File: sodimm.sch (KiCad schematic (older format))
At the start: 1 part, among them J5 2309409-1

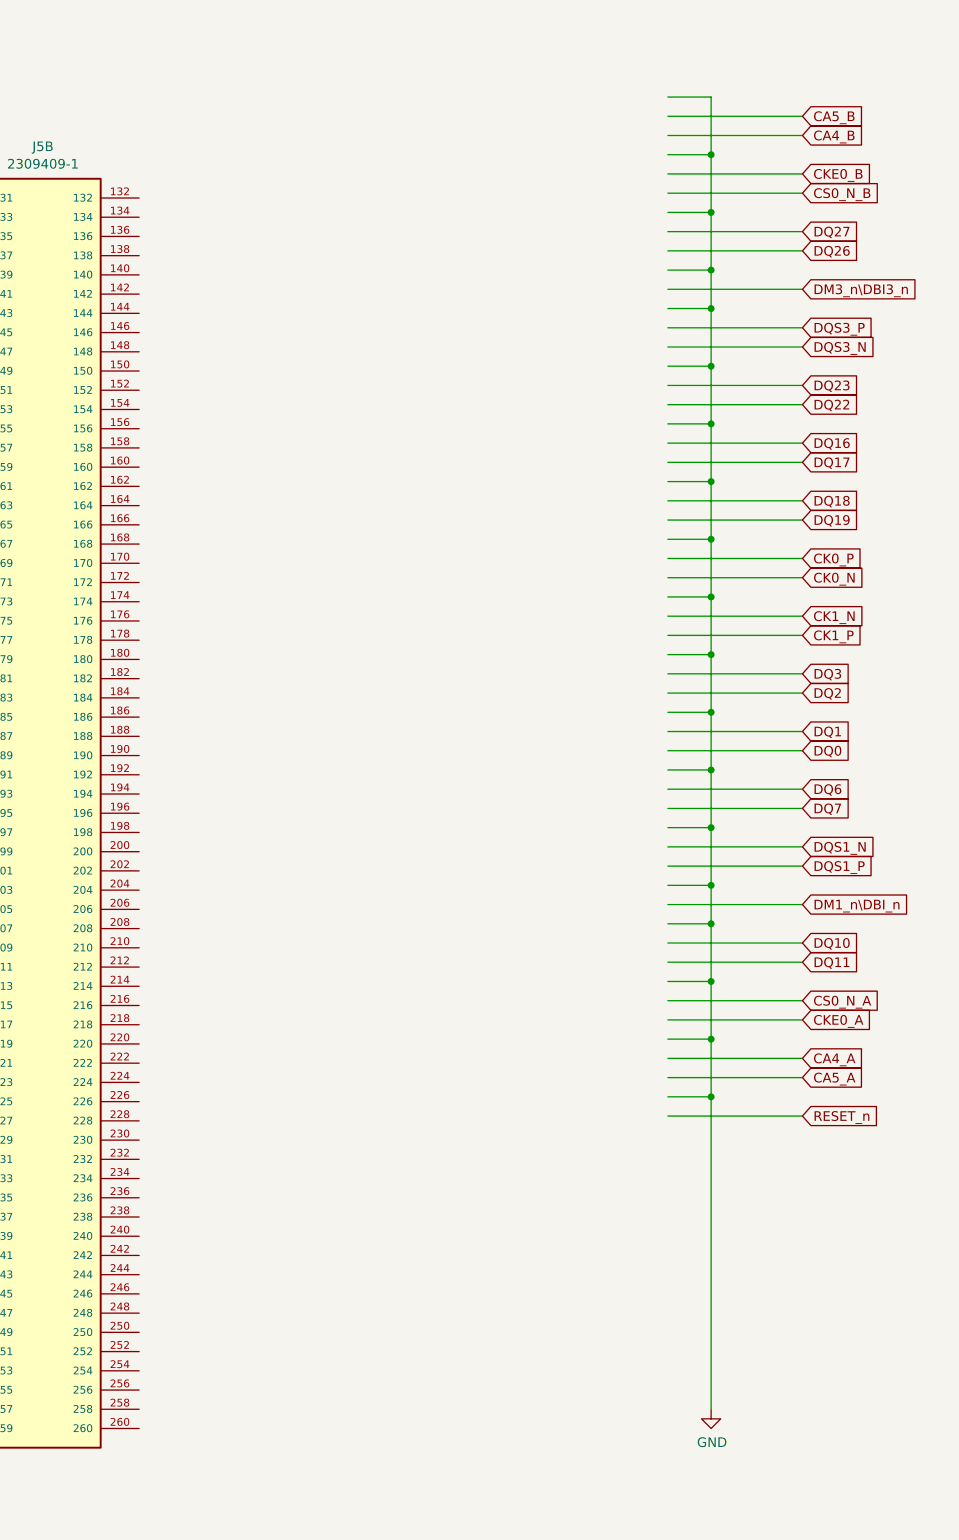
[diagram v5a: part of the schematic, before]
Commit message: Connect CA and spare IOs to SODIMM
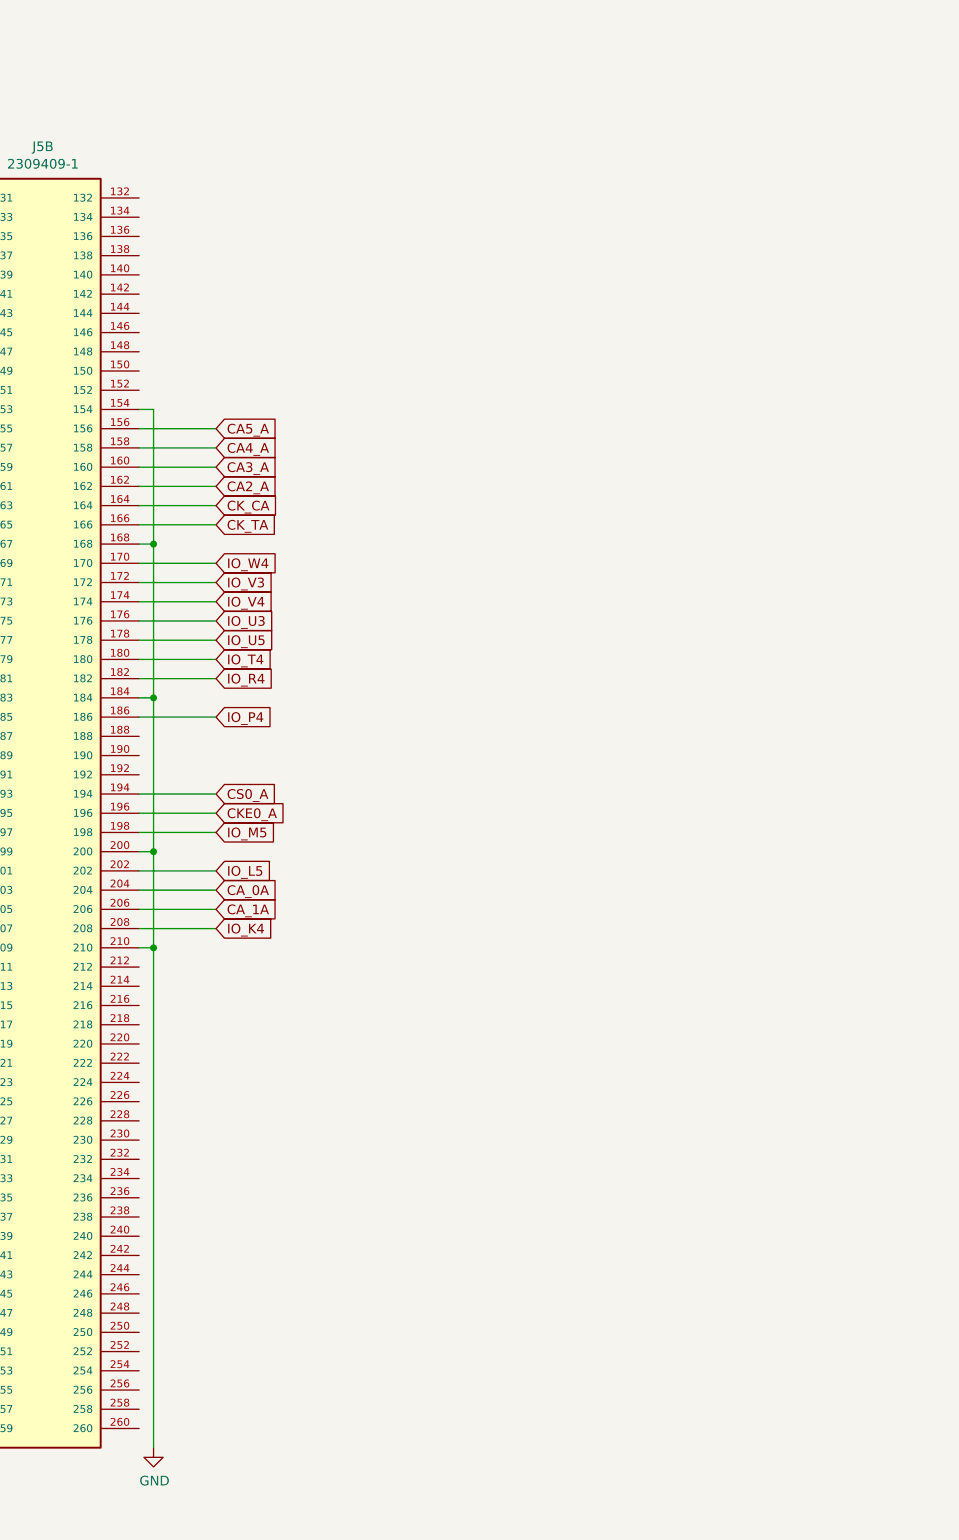
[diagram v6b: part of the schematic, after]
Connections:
- net labels added: CA_0A, CA_1A, CK_CA, CK_TA, CS0_A, IO_K4, IO_L5, IO_M5, IO_P4, IO_R4, IO_T4, IO_U3, IO_U5, IO_V3, IO_V4, IO_W4
- net labels removed: CA4_B, CA5_B, CK0_N, CK0_P, CK1_N, CK1_P, CKE0_B, CS0_N_A, CS0_N_B, DM1_n\DBI_n, DM3_n\DBI3_n, DQ0, DQ1, DQ10, DQ11, DQ16, DQ17, DQ18, DQ19, DQ2, DQ22, DQ23, DQ26, DQ27, DQ3, DQ6, DQ7, DQS1_N, DQS1_P, DQS3_N, DQS3_P, RESET_n
- wire segments 267 -> 225

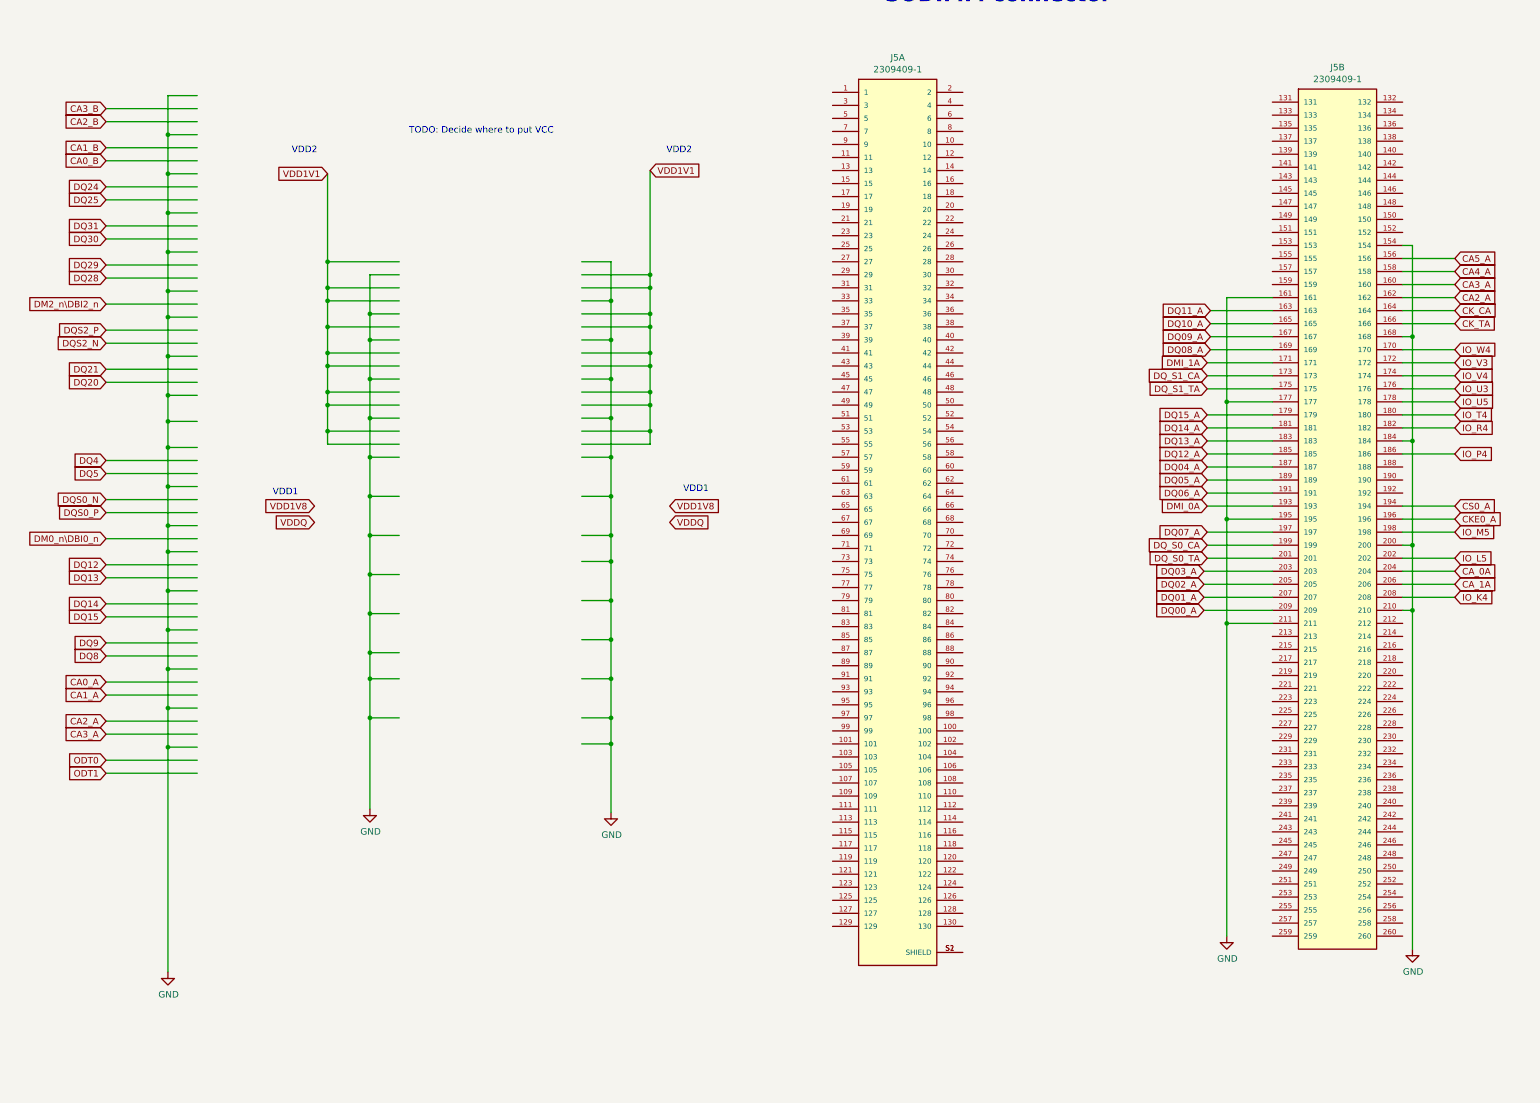
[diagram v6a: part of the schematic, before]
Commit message: Connect power supply to SO-DIMM connector
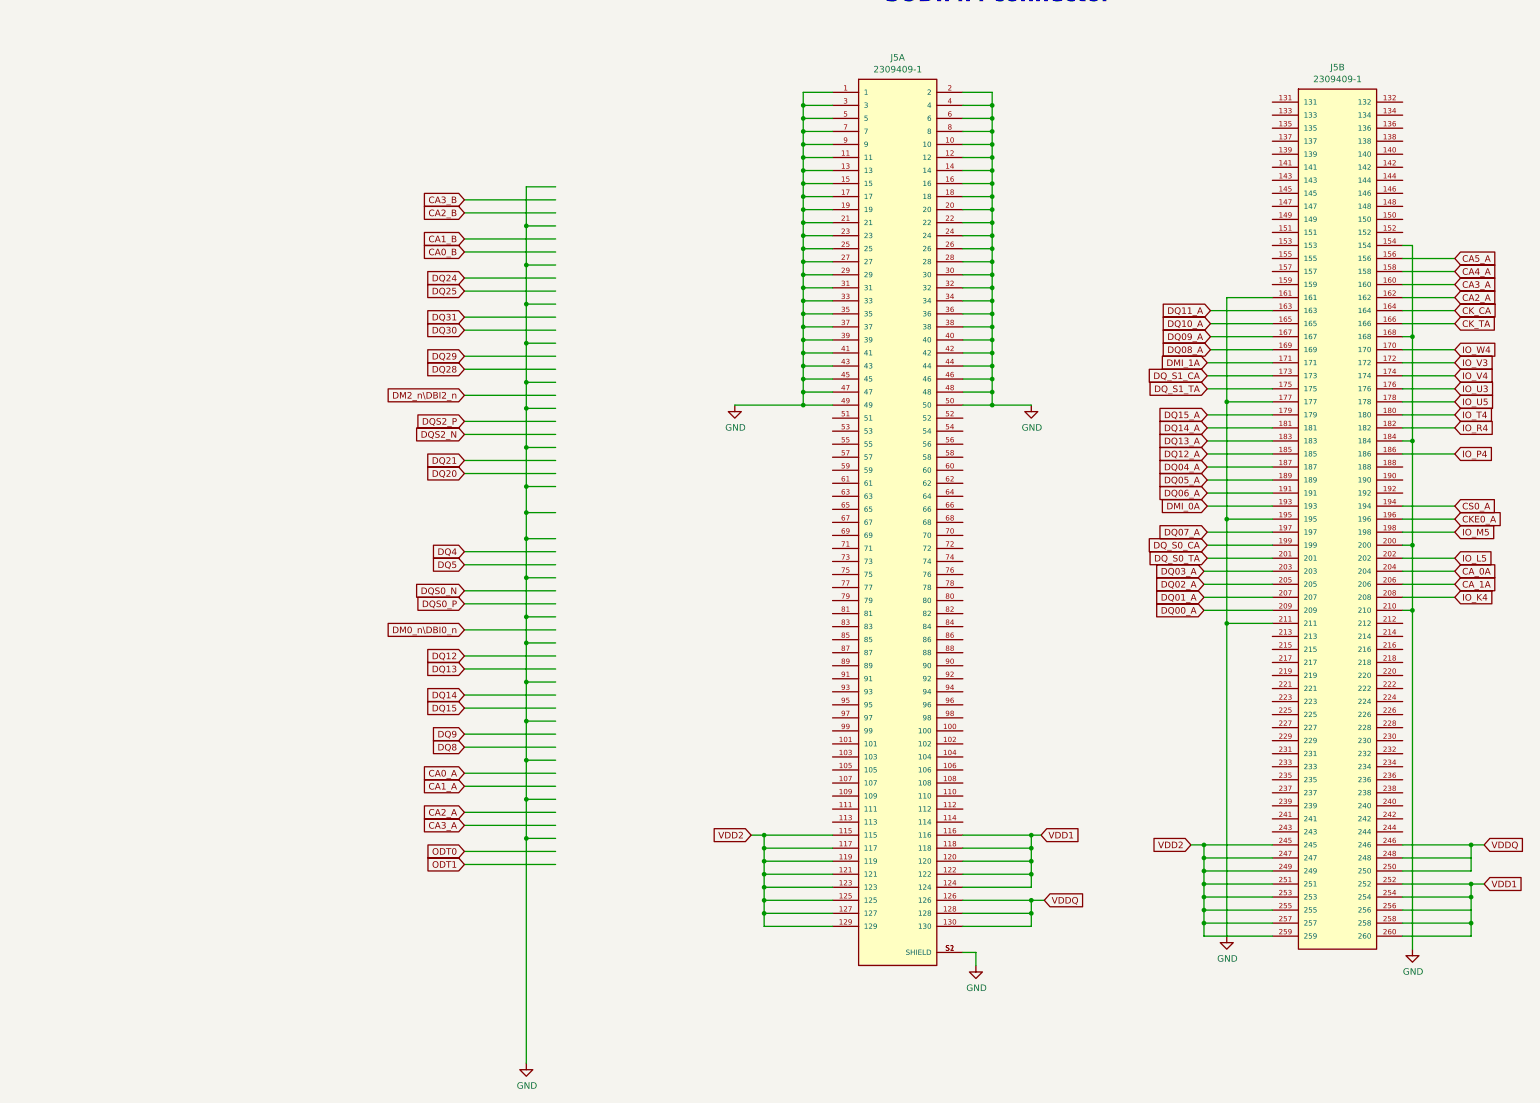
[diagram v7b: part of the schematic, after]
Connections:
- net labels added: VDD1, VDD2
- net labels removed: VDD1V1, VDD1V8
- wire segments 225 -> 297
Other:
- note removed: "TODO: Decide where to put VCC"
- note removed: "VDD1"
- note removed: "VDD2\n"
